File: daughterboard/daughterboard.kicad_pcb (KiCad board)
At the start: 2 copper layers, 51 x 39 mm, 31 parts, among them J1 Conn_02x07_Odd_Even, J2 Conn_01x01, J3 Conn_01x01, J4 Conn_01x01, J5 Conn_01x01, SW1 SW_Push, SW2 Rotary_Encoder_Switch_Alps, SW3 SW_Push, SW4 SW_Push

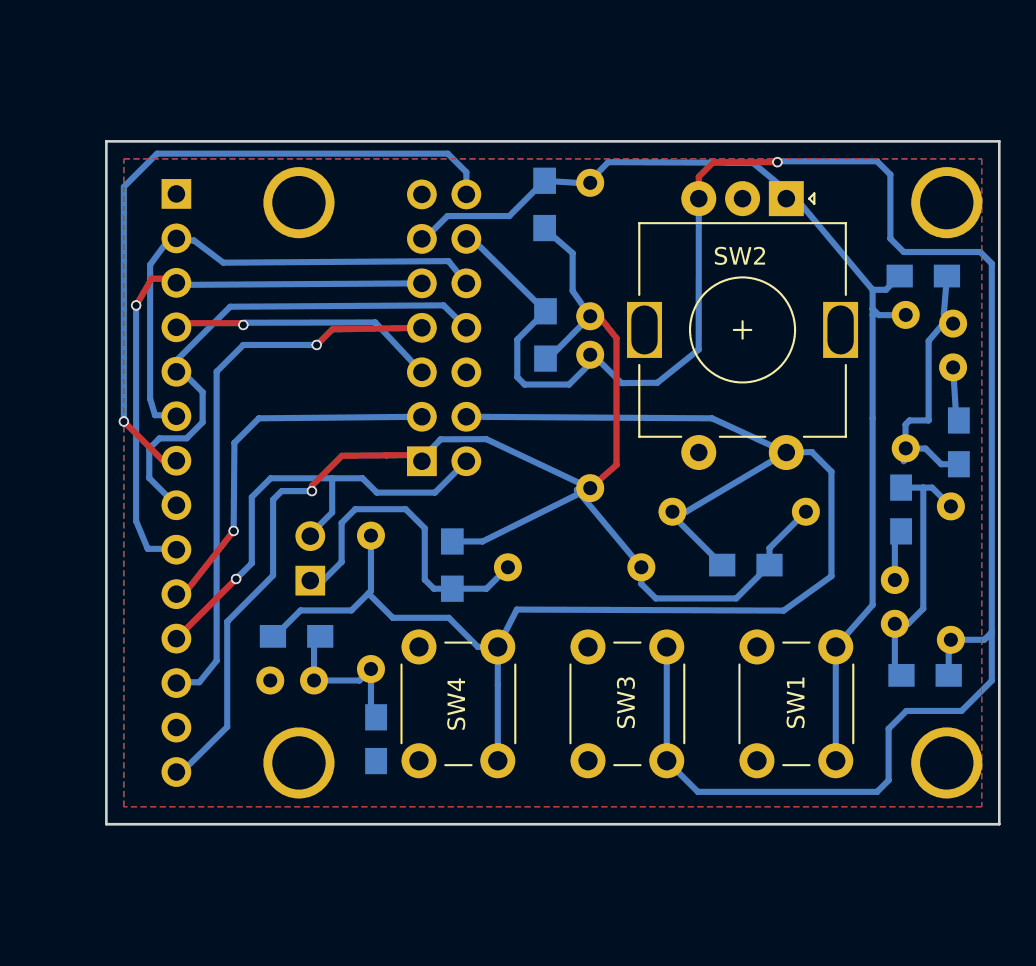
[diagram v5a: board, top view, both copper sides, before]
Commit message: Added jogwheel and sweep, simplified daughterboard
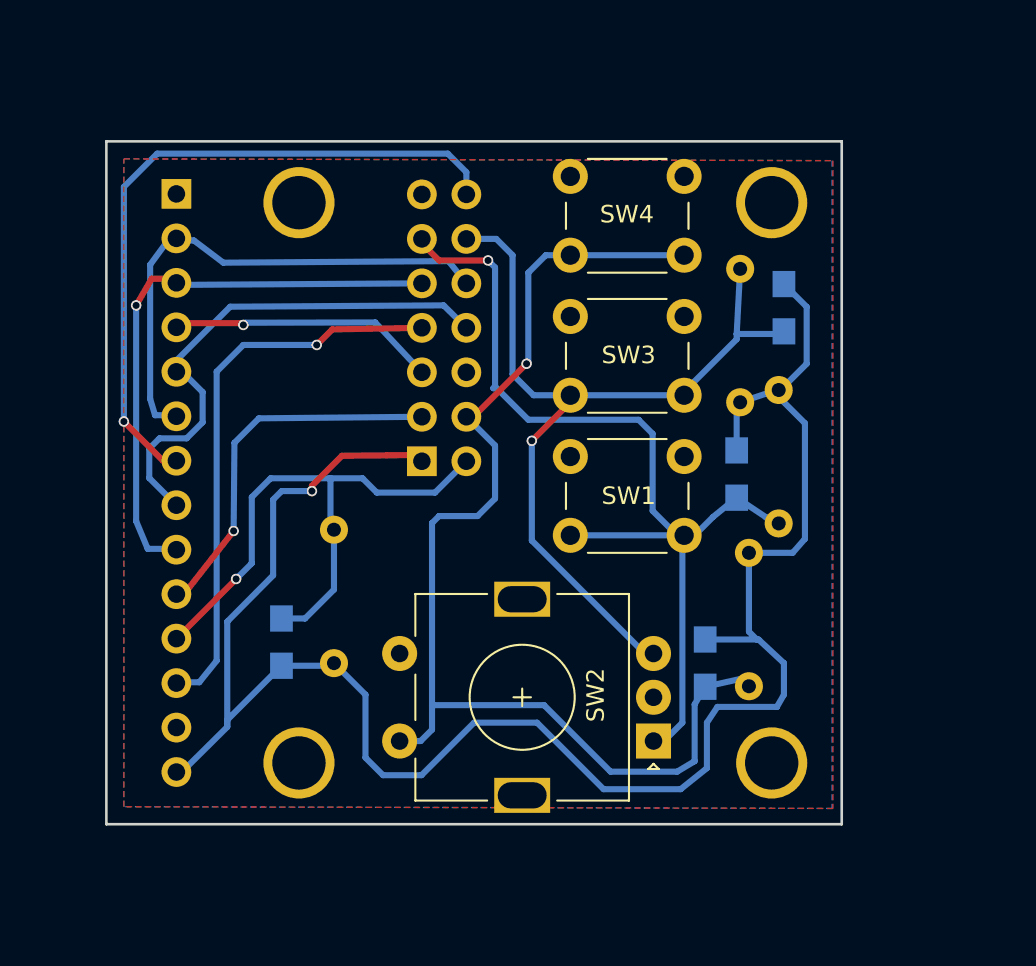
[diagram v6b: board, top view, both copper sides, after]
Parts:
- removed C1, C3, C5: 100 nF, Capacitors_SMD:C_0805_HandSoldering
- removed C2, C4, C6: 100 nF, Capacitors_THT:C_Disc_D5.0mm_W2.5mm_P2.50mm
- removed JP1: Jumper_NO_Small, Pin_Headers:Pin_Header_Straight_1x02_Pitch2.54mm
- removed R10, R12, R14: 100R, Resistors_THT:R_Axial_DIN0207_L6.3mm_D2.5mm_P7.62mm_Horizontal
- removed R11, R13, R9: 100R, Resistors_SMD:R_0805_HandSoldering
- moved SW4 34.5 mm to (126.5, 54.0), turned to 0 degrees
- moved SW2 31.9 mm to (131.2, 86.2), turned to 180 degrees
- moved SW3 25.4 mm to (126.5, 62.0), turned to 0 degrees
- moved SW1 20.4 mm to (126.5, 70.0), turned to 0 degrees
- moved R3 18.9 mm to (136.0, 71.0), turned to 270 degrees
- moved R8 18.4 mm to (113.0, 81.8), turned to 90 degrees
- moved R1 13.7 mm to (138.7, 61.5), turned to 270 degrees
- moved R4 11.6 mm to (138.4, 66.2), turned to 270 degrees
- moved R7 10.7 mm to (110.0, 80.6), turned to 90 degrees
- moved J3 10.0 mm to (138.0, 87.5)
- moved J5 10.0 mm to (138.0, 55.5)
- moved R2 9.87 mm to (136.2, 66.9)
- moved R5 6.06 mm to (134.2, 81.8), turned to 270 degrees
- moved R6 4.01 mm to (136.7, 75.5), turned to 270 degrees
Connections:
- R7 pad 2: Net-(JP1-Pad1) -> CS4
- R8 pad 2: Net-(JP1-Pad1) -> CS4
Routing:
- net INTF2: track 116.6 -> 50.9 mm
- net +5V: track 88.7 -> 110.1 mm
- net CS5: track 85.4 -> 66.9 mm, vias 0 -> 1
- net Net-(JP1-Pad1): track 18.4 -> 0.00 mm
- net Net-(C1-Pad1): track 15.7 -> 0.00 mm
- net Net-(C3-Pad1): track 15.3 -> 0.00 mm
- net Net-(C5-Pad1): track 9.42 -> 0.00 mm
- net INTF1: track 64.4 -> 55.9 mm, vias 0 -> 1
- net GND: track 6.33 -> 0.00 mm
- net CS4: track 27.5 -> 33.8 mm
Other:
- board size 51 x 39 mm -> 42 x 39 mm
